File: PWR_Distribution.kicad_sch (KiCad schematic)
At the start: 34 parts, among them IC4 AP64501QSP-13, IC8 LM76202QPWPRQ1, J1 CarPowerConnector

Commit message: added new power, but lowkey need to redo a bunch of shit
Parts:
- removed C10, C14: 10u, Capacitor_SMD:C_0805_2012Metric, symbol Device:C
- removed C54: 100n, Capacitor_SMD:C_0603_1608Metric, symbol Device:C
- removed D11: PWR FAULT, LED_SMD:LED_0603_1608Metric, symbol Device:LED
- removed D3: SD24C_SOD323, Diode_SMD:D_SOD-323, symbol Diode:SD12_SOD323
- removed IC8: LM76202QPWPRQ1, Controls_Pi:SOP65P640X120-17N, symbol LM76202QPWPRQ1:LM76202QPWPRQ1
- removed J1: CarPowerConnector, UTSVT_Connectors:Molex_Nano-Fit_105309-xx02_1x02_P2.50mm_Vertical, symbol utsvt-connectors:CarPowerConnector
- removed R40, R41, R46: 10k, Resistor_SMD:R_0805_2012Metric, symbol Device:R
- removed R42: 100k, Resistor_SMD:R_0805_2012Metric, symbol Device:R
- removed R43: 6.65k, Resistor_SMD:R_0805_2012Metric, symbol Device:R
- removed R7: 200k, Resistor_SMD:R_0805_2012Metric, symbol Device:R
- removed R8: 2k, Resistor_SMD:R_0805_2012Metric, symbol Device:R
- added C18: 1u, Capacitor_SMD:C_0603_1608Metric, symbol Device:C
- added C19: 220n, Capacitor_SMD:C_0603_1608Metric, symbol Device:C
- added C26: 22n, Capacitor_SMD:C_0603_1608Metric, symbol Device:C
- added C27: 220u, Capacitor_SMD:C_0603_1608Metric, symbol Device:C
- added IC3: LM74502HDDFR, UTSVT_Power_SP:SOT65P280X110-8N, symbol UTSVT_ICs:LM74502HDDFR
- added J1: CarLVPowerConnector, UTSVT_Connectors:Molex_Nano-Fit_105309-xx02_1x02_P2.50mm_Vertical, symbol UTSVT_Connectors:CarLVPowerConnector
- added Q1: PSMN8R5-40MSDX, UTSVT_Power_SP:PSMN8R5-40MSDX, symbol UTSVT_Power:PSMN8R5-40MSDX
- added R100: 10k, Resistor_SMD:R_0603_1608Metric, symbol Device:R_US
- added R13: 8k, Resistor_SMD:R_0603_1608Metric, symbol Device:R_US
- added R14: 200k, Resistor_SMD:R_0603_1608Metric, symbol Device:R_US
- added Z1, Z2: SMAF4751A-TP, UTSVT_Passives:SODFL5026X125N, symbol UTSVT_Power:SMAF4749A-TP
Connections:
- net +24V_PWR: now also C27.1, IC3.8 (SRC), Q1.10 (D_6), Q1.11 (D_7), Q1.5 (D_1), Q1.6 (D_2), Q1.7 (D_3), Q1.8 (D_4), Q1.9 (D_5)
- net GND: now also C18.1, C27.2, IC3.2 (GND), J1.2 (GND), R13.2, Z1.2 (A), Z2.2 (A)
- new net: C26.1, IC3.6 (GATE), Q1.4 (G)
- new net: C19.2, IC3.4 (VCAP)
- new net: IC3.7 (OV), R13.1, R14.2
- new net LV+: C26.2, J1.1 (+24V), Q1.1 (S_1), Q1.2 (S_2), Q1.3 (S_3), R100.1, R14.1, Z2.1 (K)
- new net RPP_EN: C18.2, C19.1, IC3.1 (EN/UVLO), IC3.5 (VS), R100.2, Z1.1 (K)
- no-connect marks 3 -> 0
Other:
- note added: "Power"
- note added: "RPP & OVP From VCU"
- note removed: "Current lim(A) = 12/Rilim(k) 1.8A = 12/6.65k ohms"
- note removed: "RTN!=GND Conecting GND to RTN turns off RPP!"
- note removed: "Should be ok for 24V?"
- note removed: "Someone plz double check"
- note removed: "These have been changed from 12V to 24V values R7: 100k -> 200k R8: 200 -> 2k R40: 1k -> 10k OVP = ~25V, UVLO = ~21V (?) D3: SD12 -> SD24C"
- note removed: "UVLO: ~1.19 = 21 * (R8+R40)/(R7+R8+R40) OVP: ~1.19 = 25 * R40/(R7+R8+R40)"
- note removed: "Vin protection"
- moved on the sheet: C5, C56, C58, C59, C6, C60, C61, C7, C8, C9, D7, D9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

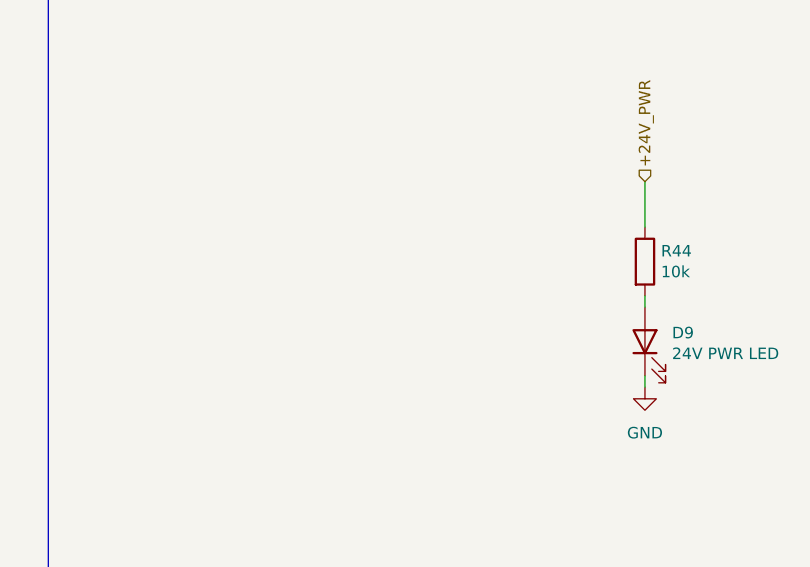
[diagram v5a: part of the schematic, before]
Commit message: ready to route high speed i believe
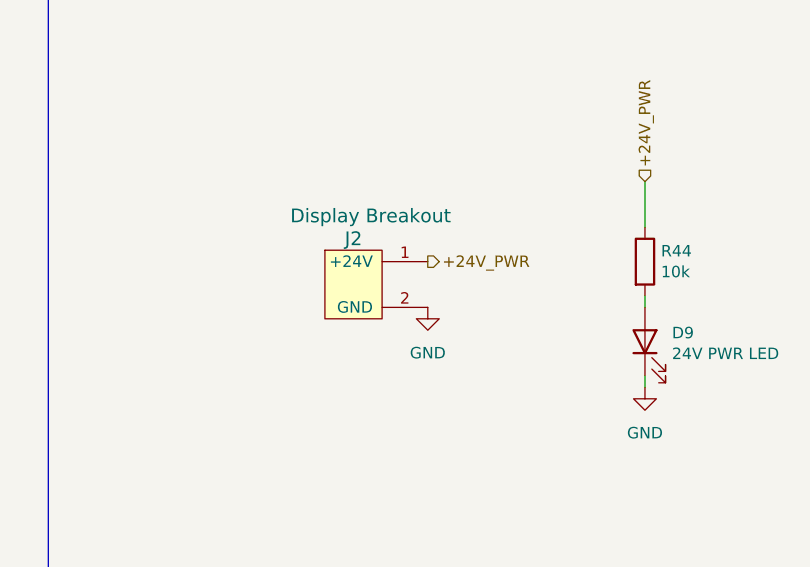
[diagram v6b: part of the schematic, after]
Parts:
- added J2: Display Breakout, UTSVT_Connectors:Molex_Nano-Fit_105309-xx02_1x02_P2.50mm_Vertical, symbol UTSVT_Connectors:CarLVPowerConnector
- R44: footprint Resistor_SMD:R_0805_2012Metric -> Resistor_SMD:R_0603_1608Metric
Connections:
- net +24V_PWR: now also J2.1 (+24V)
- net GND: now also J2.2 (GND)
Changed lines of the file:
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@@
+	(hierarchical_label "+24V_PWR"
+		(shape output)
+		(at 184.15 62.23 0)
+		(effects
+			(font
+				(size 1.27 1.27)
+			)
+			(justify left)
+		)
+	)
 	(hierarchical_label "+24V_PWR"
 		(shape output)
@@
 			)
 		)
-		(property "Footprint" "Resistor_SMD:R_0805_2012Metric"
+		(property "Footprint" "Resistor_SMD:R_0603_1608Metric"
 			(at 206.502 62.23 90)
 			(effects
@@
 	(symbol
 		(lib_id "power:GND")
+		(at 184.15 67.31 0)
+		(unit 1)
+		(exclude_from_sim no)
+		(in_bom yes)
+		(on_board yes)
+		(dnp no)
+		(fields_autoplaced yes)
+		(property "Reference" "#PWR04"
+			(at 184.15 73.66 0)
+			(effects
+				(font
+					(size 1.27 1.27)
+				)
+				(hide yes)
+			)
+		)
+		(property "Value" "GND"
+			(at 184.15 72.39 0)
+			(effects
+				(font
+					(size 1.27 1.27)
+				)
+			)
+		)
+		(property "Footprint" ""
+			(at 184.15 67.31 0)
+			(effects
+				(font
+					(size 1.27 1.27)
+				)
+				(hide yes)
+			)
+		)
+		(property "Datasheet" ""
+			(at 184.15 67.31 0)
+			(effects
+				(font
+					(size 1.27 1.27)
+				)
+				(hide yes)
+			)
+		)
+		(property "Description" "Power symbol creates a global label with name \"GND\" , ground"
+			(at 184.15 67.31 0)
+			(effects
+				(font
+					(size 1.27 1.27)
+				)
+				(hide yes)
+			)
+		)
+		(pin "1"
+		)
+		(instances
+			(project "PiBoard"
+				(path "/e4d65698-b8ec-4bf6-9f2b-a5010377155a/0c1fd794-8ba7-4f58-ad3e-1ee234c84a43"
+					(reference "#PWR04")
+					(unit 1)
+				)
+			)
+		)
+	)
+	(symbol
+		(lib_id "power:GND")
 		(at 116.84 157.48 0)
 		(unit 1)
@@
 					(unit 1)
 				)
+			)
+		)
+	)
+	(symbol
+		(lib_id "UTSVT_Connectors:CarLVPowerConnector")
+		(at 176.53 64.77 0)
+		(unit 1)
+		(exclude_from_sim no)
+		(in_bom yes)
+		(on_board yes)
+		(dnp no)
+		(property "Reference" "J2"
+			(at 175.895 59.69 0)
+			(effects
+				(font
+					(size 1.524 1.524)
+				)
+			)
+		)
+		(property "Value" "Display Breakout"
+			(at 177.8 57.15 0)
+			(effects
+				(font
+					(size 1.524 1.524)
+				)
+			)
+		)
+		(property "Footprint" "UTSVT_Connectors:Molex_Nano-Fit_105309-xx02_1x02_P2.50mm_Vertical"
+			(at 176.53 64.77 0)
+			(effects
+				(font
+					(size 1.524 1.524)
+				)
+				(hide yes)
+			)
+		)
+		(property "Datasheet" ""
+			(at 176.53 64.77 0)
+			(effects
+				(font
+					(size 1.524 1.524)
+				)
+				(hide yes)
+			)
+		)
+		(property "Description" "Connector for the car's 24V power bus"
+			(at 176.53 64.77 0)
+			(effects
+				(font
+					(size 1.27 1.27)
+				)
+				(hide yes)
+			)
+		)
+		(property "P/N" ""
+			(at 176.53 64.77 0)
+			(effects
+				(font
+					(size 1.27 1.27)
+				)
+				(hide yes)
+			)
+		)
+		(pin "1"
+		)
+		(pin "2"
+		)
+		(instances
+			(project "PiBoard"
+				(path "/e4d65698-b8ec-4bf6-9f2b-a5010377155a/0c1fd794-8ba7-4f58-ad3e-1ee234c84a43"
+					(reference "J2")
+					(unit 1)
+				)

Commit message: changed a bunch of stuff, still have work
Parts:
- C6: value 100n -> 10uF
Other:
- note added: "R: ~11000"
- note added: "R: ~1500"
- note added: "fwd cur: ~2ma fwd volt: ~2V"
- moved on the sheet: C58, C6
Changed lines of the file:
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@@
 		)
 	)
+	(text "R: ~1500"
+		(exclude_from_sim no)
+		(at 236.982 57.404 0)
+		(effects
+			(font
+				(size 1.27 1.27)
+			)
+		)
+	)
 	(text "+5v @ 5A PSU ( 7.5v-28v Input )"
 		(exclude_from_sim no)
@@
 		)
 	)
+	(text "R: ~11000"
+		(exclude_from_sim no)
+		(at 214.884 57.658 0)
+		(effects
+			(font
+				(size 1.27 1.27)
+			)
+		)
+	)
+	(text "fwd cur: ~2ma\nfwd volt: ~2V\n"
+		(exclude_from_sim no)
+		(at 218.948 46.736 0)
+		(effects
+			(font
+				(size 1.27 1.27)
+			)
+		)
+	)
 	(text "Power"
 		(exclude_from_sim no)
@@
 	)
 	(junction
+		(at 30.48 149.86)
+		(diameter 0)
+		(color 0 0 0 0)
+	)
+	(junction
 		(at 99.695 49.53)
 		(diameter 0)
@@
 	)
 	(junction
-		(at 31.75 148.59)
-		(diameter 0)
-		(color 0 0 0 0)
-	)
-	(junction
 		(at 44.45 130.81)
 		(diameter 0)
@@
 	)
 	(junction
-		(at 31.75 140.97)
+		(at 55.88 81.28)
 		(diameter 0)
 		(color 0 0 0 0)
 	)
 	(junction
-		(at 55.88 81.28)
+		(at 30.48 139.7)
 		(diameter 0)
 		(color 0 0 0 0)
@@
 	(wire
 		(pts
-			(xy 22.86 140.97) (xy 31.75 140.97)
+			(xy 30.48 139.7) (xy 30.48 140.97)
+		)
+		(stroke
+			(width 0)
+			(type default)
+		)
+	)
+	(wire
+		(pts
+			(xy 21.59 139.7) (xy 30.48 139.7)
 		)
 		(stroke
@@
 	(wire
 		(pts
-			(xy 31.75 148.59) (xy 31.75 149.86)
-		)
-		(stroke
-			(width 0)
-			(type default)
-		)
-	)
-	(wire
-		(pts
 			(xy 208.28 67.31) (xy 208.28 66.04)
 		)
@@
 	(wire
 		(pts
-			(xy 31.75 140.97) (xy 31.75 139.7)
+			(xy 116.84 148.59) (xy 116.84 157.48)
 		)
 		(stroke
@@
 	(wire
 		(pts
-			(xy 116.84 148.59) (xy 116.84 157.48)
+			(xy 134.62 139.7) (xy 146.05 139.7)
 		)
 		(stroke
@@
 	(wire
 		(pts
-			(xy 134.62 139.7) (xy 146.05 139.7)
+			(xy 55.88 80.645) (xy 55.88 81.28)
 		)
 		(stroke
@@
 	(wire
 		(pts
-			(xy 55.88 80.645) (xy 55.88 81.28)
+			(xy 80.01 129.54) (xy 80.01 127)
 		)
 		(stroke
@@
 	(wire
 		(pts
-			(xy 80.01 129.54) (xy 80.01 127)
+			(xy 30.48 149.86) (xy 34.29 149.86)
 		)
 		(stroke
@@
 	(wire
 		(pts
-			(xy 22.86 148.59) (xy 31.75 148.59)
+			(xy 21.59 149.86) (xy 30.48 149.86)
 		)
 		(stroke
@@
 	(wire
 		(pts
-			(xy 46.99 148.59) (xy 46.99 149.86)
+			(xy 21.59 139.7) (xy 21.59 140.97)
 		)
 		(stroke
@@
 	(wire
 		(pts
-			(xy 44.45 130.81) (xy 44.45 132.08)
+			(xy 46.99 148.59) (xy 46.99 149.86)
 		)
 		(stroke
 			(width 0)
-			(type solid)
+			(type default)
 		)
 	)
 	(wire
 		(pts
-			(xy 99.695 41.91) (xy 99.695 44.45)
+			(xy 44.45 130.81) (xy 44.45 132.08)
 		)
 		(stroke
 			(width 0)
-			(type default)
+			(type solid)
 		)
 	)
 	(wire
 		(pts
-			(xy 34.29 130.81) (xy 44.45 130.81)
+			(xy 99.695 41.91) (xy 99.695 44.45)
 		)
 		(stroke
@@
 	(wire
 		(pts
-			(xy 36.83 139.7) (xy 36.83 140.97)
+			(xy 34.29 130.81) (xy 44.45 130.81)
 		)
 		(stroke
@@
 	(wire
 		(pts
-			(xy 99.695 41.91) (xy 104.775 41.91)
+			(xy 36.83 139.7) (xy 36.83 140.97)
 		)
 		(stroke
@@
 	(wire
 		(pts
-			(xy 31.75 149.86) (xy 34.29 149.86)
+			(xy 99.695 41.91) (xy 104.775 41.91)
 		)
 		(stroke
@@
 	(wire
 		(pts
+			(xy 21.59 149.86) (xy 21.59 148.59)
+		)
+		(stroke
+			(width 0)
+			(type default)
+		)
+	)
+	(wire
+		(pts
 			(xy 116.84 129.54) (xy 134.62 129.54)
 		)
@@
 	(wire
 		(pts
+			(xy 30.48 139.7) (xy 34.29 139.7)
+		)
+		(stroke
+			(width 0)
+			(type default)
+		)
+	)
+	(wire
+		(pts
 			(xy 64.135 72.39) (xy 67.31 72.39)
 		)
@@
 	(wire
 		(pts
-			(xy 31.75 139.7) (xy 34.29 139.7)
-		)
-		(stroke
-			(width 0)
-			(type default)
-		)
-	)
-	(wire
-		(pts
 			(xy 104.14 64.77) (xy 104.14 65.405)
 		)
@@
 	(wire
 		(pts
+			(xy 30.48 149.86) (xy 30.48 148.59)
+		)
+		(stroke
+			(width 0)
+			(type default)
+		)
+	)
+	(wire
+		(pts
 			(xy 116.84 138.43) (xy 116.84 139.7)
 		)
@@
 	(symbol
 		(lib_id "Device:C")
-		(at 31.75 144.78 0)
+		(at 30.48 144.78 0)
 		(unit 1)
 		(exclude_from_sim no)
@@
 		(dnp no)
 		(property "Reference" "C6"
-			(at 27.178 142.748 0)
+			(at 25.908 142.748 0)
 			(effects
 				(font
@@
 			)
 		)
-		(property "Value" "100n"
-			(at 25.908 146.558 0)
+		(property "Value" "10uF"
+			(at 24.638 146.558 0)
 			(effects
 				(font
@@
 		)
 		(property "Footprint" "Capacitor_SMD:C_0603_1608Metric"
-			(at 32.7152 148.59 0)
+			(at 31.4452 148.59 0)
 			(effects
 				(font
@@
 		)
 		(property "Datasheet" ""
-			(at 31.75 144.78 0)
+			(at 30.48 144.78 0)
 			(effects
 				(font
@@
 		)
 		(property "Description" "Unpolarized capacitor"
-			(at 31.75 144.78 0)
+			(at 30.48 144.78 0)
 			(effects
 				(font
@@
 		)
 		(property "P/N" "C0805C104M5RACTU"
-			(at 31.75 144.78 0)
+			(at 30.48 144.78 0)
 			(effects
 				(font
@@
 	(symbol
 		(lib_id "Device:C")
-		(at 22.86 144.78 0)
+		(at 21.59 144.78 0)
 		(unit 1)
 		(exclude_from_sim no)
@@
 		(dnp no)
 		(property "Reference" "C58"
-			(at 13.97 143.4846 0)
+			(at 12.7 143.4846 0)
 			(effects
 				(font
@@
 		)
 		(property "Value" "10uF"
-			(at 13.97 145.796 0)
+			(at 12.7 145.796 0)
 			(effects
 				(font
@@
 		)
 		(property "Footprint" "Capacitor_SMD:C_0805_2012Metric"
-			(at 23.8252 148.59 0)
+			(at 22.5552 148.59 0)
 			(effects
 				(font
@@
 		)
 		(property "Datasheet" "~"
-			(at 22.86 144.78 0)
+			(at 21.59 144.78 0)
 			(effects
 				(font
@@
 		)
 		(property "Description" "Unpolarized capacitor"
-			(at 22.86 144.78 0)
+			(at 21.59 144.78 0)
 			(effects
 				(font
@@
 		)
 		(property "P/N" "0805W106K500CC"
-			(at 22.86 144.78 0)
+			(at 21.59 144.78 0)
 			(effects
 				(font

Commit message: my life is horrible
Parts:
- R13: value 8k -> 10k
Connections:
- net +24V_PWR renamed +24V
- net +5V_PWR renamed +5V
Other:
- note added: "24V -> 5V BUCK"
- note added: "Est. max power draw (CM5) = 10W (pi) + 1.5W (HDMI) + 0.6W (CAN) = ~12.1W (rest of board draws negligible power)"
- note added: "LEDS"
- note added: "Should be spec'd for CM5?"
- note added: "fuse here"
- note added: "~26V OVP"
- moved on the sheet: C18, C19, C26, C27, C5, C56, C58, C59, C6, C60, C61, C7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
